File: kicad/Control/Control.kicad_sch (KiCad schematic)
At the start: 66 parts, among them J3 Control Connector, J4 Data Connector, U1 27C64, U10 74LS377, U11 74LS253, U12 74LS253, U13 74LS253, U14 74LS253, U15 74LS253, U16 74LS253, U17 74LS253, U18 74LS257, U19 74LS377, U2 27C64, U20 74LS377, U21 74LS377, U22 74LS138, U23 74LS32, U24 74LS08, U25 74LS86, U26 74LS74, U3 27C64, U4 27C64, U5 27C64, U6 74LS273, U7 74LS377, U8 74LS377, U9 74LS377

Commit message: Start work on memory / addressing board
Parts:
- renumbered J3 to J1, J4 to J2
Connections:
- net WRITE_CORE renamed *WRITE_CORE
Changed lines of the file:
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@@
     (effects (font (size 1.27 1.27)) (justify right bottom))
   )
-  (label "WRITE_CORE" (at 471.805 104.775 180) (fields_autoplaced)
+  (label "*WRITE_CORE" (at 471.805 104.775 180) (fields_autoplaced)
     (effects (font (size 1.27 1.27)) (justify right bottom))
   )
@@
     (effects (font (size 1.27 1.27)) (justify left bottom))
   )
-  (label "WRITE_CORE" (at 155.575 127 0) (fields_autoplaced)
+  (label "*WRITE_CORE" (at 155.575 127 0) (fields_autoplaced)
     (effects (font (size 1.27 1.27)) (justify left bottom))
   )
@@
   (symbol (lib_id "Connector:DIN41612_02x32_AC") (at 476.885 273.685 0) (unit 1)
     (in_bom yes) (on_board yes) (dnp no)
-    (property "Reference" "J4" (at 478.155 233.045 0)
+    (property "Reference" "J2" (at 478.155 233.045 0)
       (effects (font (size 1.27 1.27)))
     )
@@
       (project "Control"
         (path "/9aceca4c-796d-4c9d-8044-fc5cfdda262d"
-          (reference "J4") (unit 1)
+          (reference "J2") (unit 1)
         )
       )
@@
   (symbol (lib_id "Connector:DIN41612_02x32_AC") (at 476.885 89.535 0) (unit 1)
     (in_bom yes) (on_board yes) (dnp no)
-    (property "Reference" "J3" (at 478.155 48.895 0)
+    (property "Reference" "J1" (at 478.155 48.895 0)
       (effects (font (size 1.27 1.27)))
     )
@@
       (project "Control"
         (path "/9aceca4c-796d-4c9d-8044-fc5cfdda262d"
-          (reference "J3") (unit 1)
+          (reference "J1") (unit 1)
         )
       )

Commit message: Continue work on memory board
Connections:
- net EXTRA7 renamed NEXT_BANK0
- net EXTRA8 renamed NEXT_BANK1
- net REST_PEND renamed *REST_PEND

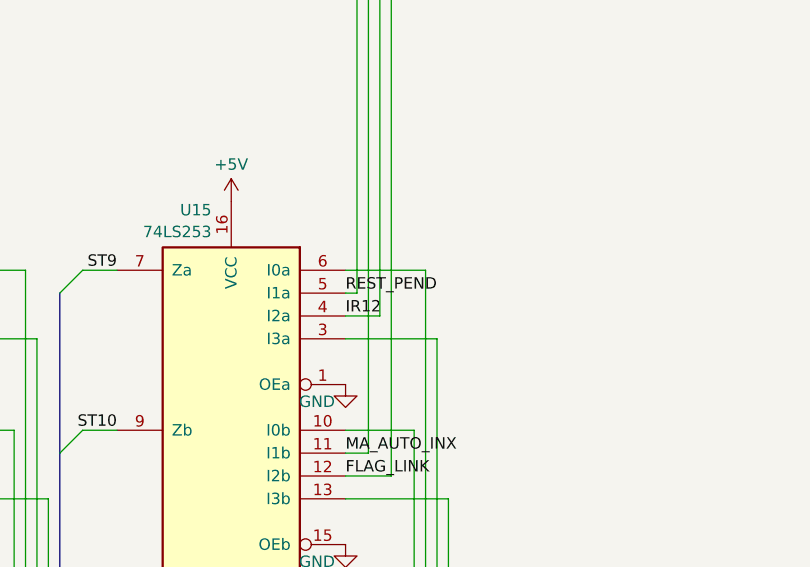
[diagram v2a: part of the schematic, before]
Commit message: Finish pinout audit + fanout correction
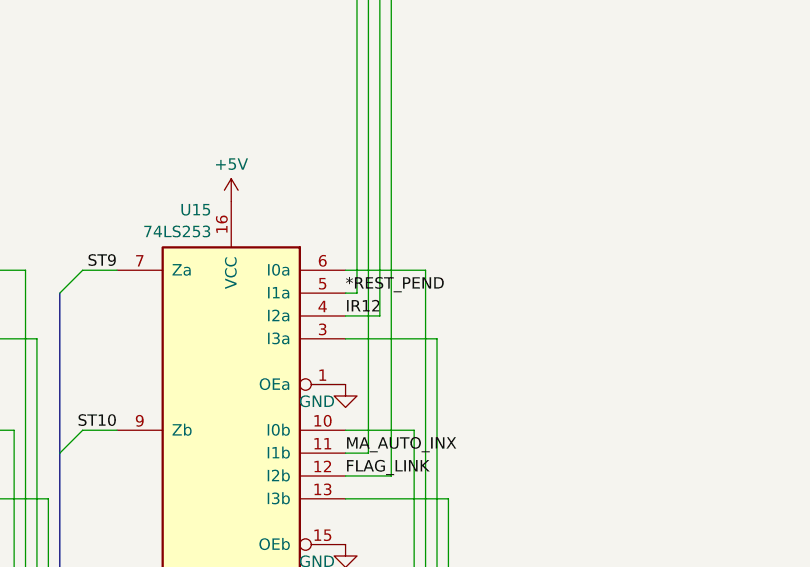
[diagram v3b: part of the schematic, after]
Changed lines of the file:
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@@
     (effects (font (size 1.27 1.27)) (justify left bottom))
   )
-  (label "REST_PEND" (at 266.065 220.98 0) (fields_autoplaced)
+  (label "*REST_PEND" (at 266.065 220.98 0) (fields_autoplaced)
     (effects (font (size 1.27 1.27)) (justify left bottom))
   )
